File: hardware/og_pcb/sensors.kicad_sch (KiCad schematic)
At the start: 19 parts, among them J2 Conn_Coaxial, U1 CD-PA1616D, U13 INA219AxD, U15 TMP1075DSG

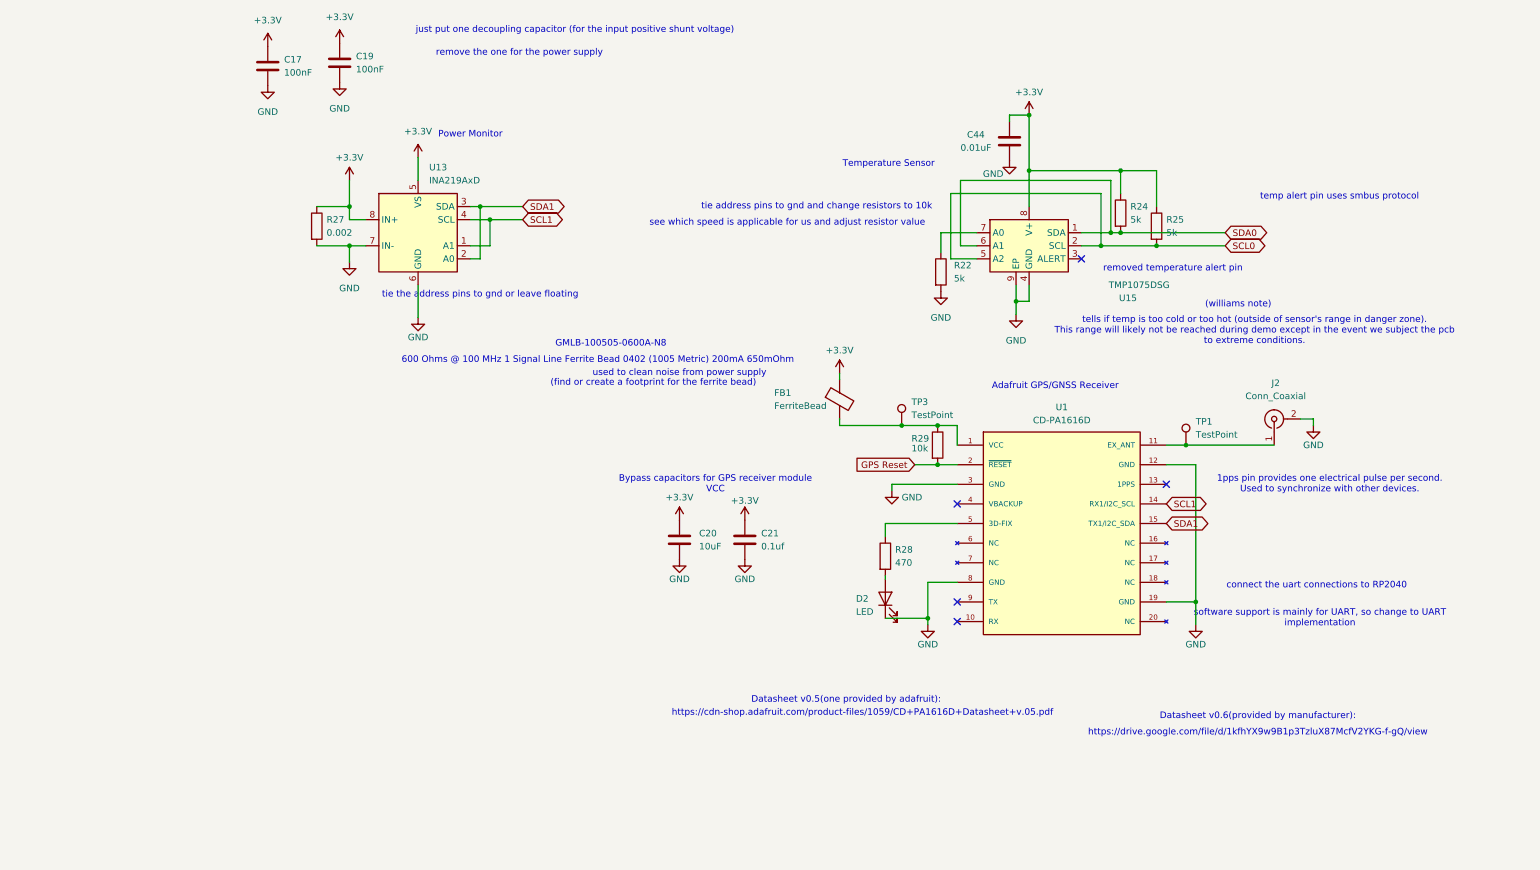
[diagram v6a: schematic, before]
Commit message: implemented pragun's advice
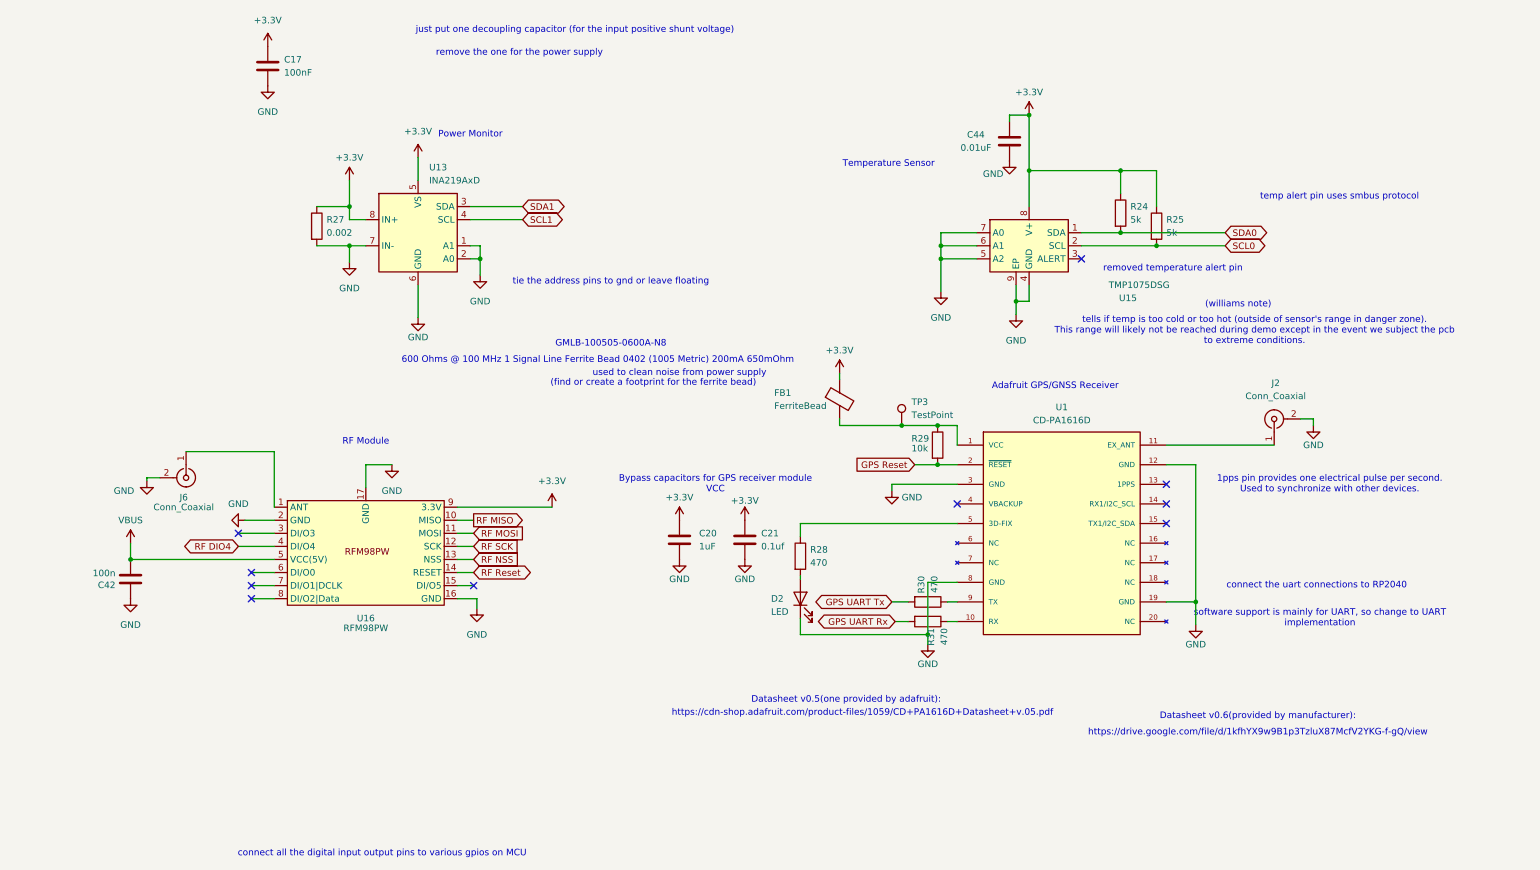
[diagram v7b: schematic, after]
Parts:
- removed C19: 100nF, Capacitor_SMD:C_0402_1005Metric, symbol Device:C
- removed R22: 5k, Resistor_SMD:R_0402_1005Metric, symbol Device:R
- removed TP1: TestPoint, 1my_footprints:TestPoint_Loop_D1.80mm_Drill1.0mm_Beaded, symbol Connector:TestPoint
- added C42: 100n, Capacitor_SMD:C_0402_1005Metric, symbol Device:C
- added J6: Conn_Coaxial, Connector_Coaxial:MMCX_Molex_73415-1471_Vertical, symbol Connector:Conn_Coaxial
- added R30, R31: 470, Resistor_SMD:R_0402_1005Metric, symbol Device:R
- added U16: RFM98PW, 1my_footprints:RFM98PW, symbol 1my_symbol:RF_Module
- C20: value 10uF -> 1uF
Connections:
- net +3.3V: now also U16.9 (3.3V)
- net GND: now also U13.1 (A1), U13.2 (A0), U15.5 (A2), U15.6 (A1), U15.7 (A0), C42.1, J6.2 (Ext), U16.16 (GND), U16.17 (GND), U16.2 (GND)
- net SCL0: no longer U15.5 (A2)
- net SCL1: no longer U1.14 (RX1/I2C_SCL), U13.1 (A1)
- net SDA0: no longer U15.6 (A1)
- net SDA1: no longer U1.15 (TX1/I2C_SDA), U13.2 (A0)
- net at U1.10 (RX): now also R31.1
- net at U1.9 (TX): now also R30.1
- new net: J6.1 (In), U16.1 (ANT)
- new net GPS UART Rx: R31.2
- new net GPS UART Tx: R30.2
- new net RF DIO4: U16.4 (DI/O4)
- new net RF MISO: U16.10 (MISO)
- new net RF MOSI: U16.11 (MOSI)
- new net RF NSS: U16.13 (NSS)
- new net RF Reset: U16.14 (RESET)
- new net RF SCK: U16.12 (SCK)
- new net VBUS: C42.2, U16.5 (VCC(5V))
- no-connect marks 5 -> 10
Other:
- note added: "RF Module"
- note added: "connect all the digital input output pins to various gpios on MCU"
- note removed: "see which speed is applicable for us and adjust resistor value"
- note removed: "tie address pins to gnd and change resistors to 10k"
- moved on the sheet: D2, R28
